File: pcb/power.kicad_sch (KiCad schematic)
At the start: 13 parts

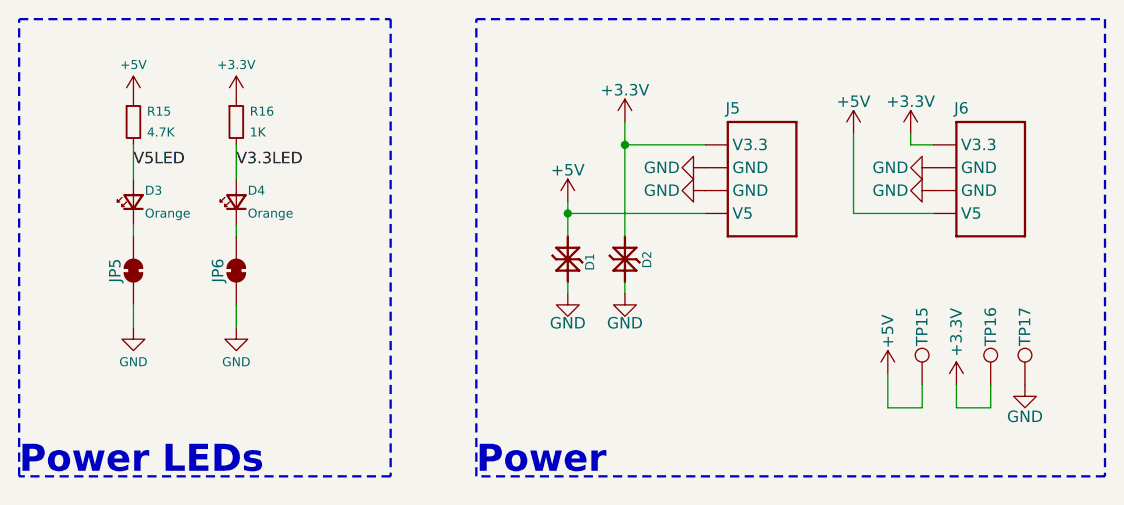
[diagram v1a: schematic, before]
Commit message: Redesign with cutouts for sensors
Removed power connectors since 5V is not needed
Added cutout for VOC sensor
Rerouted sensor section
Rescaled logos and fixed silkscreen
Changed to blue LED for power indicator
Updated requirements and renders
Changed all 0.1uF caps to small symbol
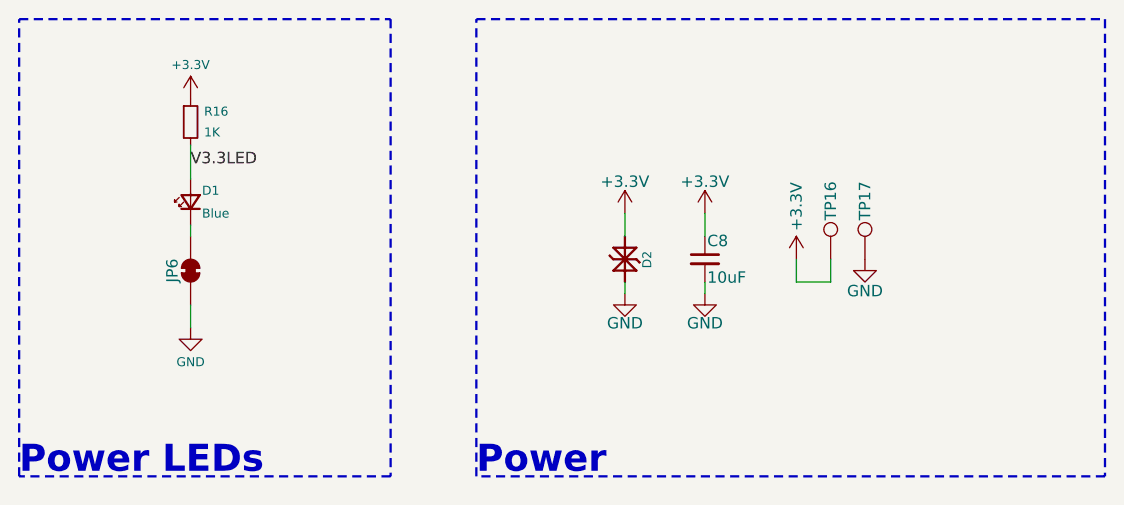
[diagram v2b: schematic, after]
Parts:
- removed D1: PESD5V5C1BL, CRGM Passive:DFN1006-2, symbol CRGM Passive:PESD5V5C1BLYL
- removed D3, D4: Orange, CRGM Passive:LED_0603_1608Metric, symbol Device:LED_Small
- removed J5, J6: ~, CRGM Connector:JST_SH_SM04B-SRSS-TB_1x04-1MP_P1.00mm_Horizontal, symbol CRGM Connector:AQ_POWER
- removed JP5: ~, CRGM Connector:SolderJumper-2_P1.3mm_Bridged_RoundedPad1.0x1.5mm, symbol Jumper:SolderJumper_2_Bridged
- removed R15: 4.7K, CRGM Passive:R_0603_1608Metric, symbol Device:R_Small
- removed TP15: ~, CRGM Mechanical:TestPoint_Pad_D1.0mm, symbol CRGM Connector:TestPoint
- added C8: 10uF, CRGM Passive:C_0603_1608Metric, symbol Device:C_Small
- added D1: Blue, CRGM Passive:LED_0603_1608Metric, symbol Device:LED_Small
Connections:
- net +3.3V: now also C8.1
- net GND: now also C8.2
- net V3.3LED: now also D1.2 (A)
- net at JP6.2 (B): now also D1.1 (K)
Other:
- moved on the sheet: JP6, R16, TP16, TP17

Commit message: Adjusted spacing and alignment of parts
Moved temp and voc to be on grid
Updated renders
Ran ERC -- fixed errors
Ran DRC -- fixed errors
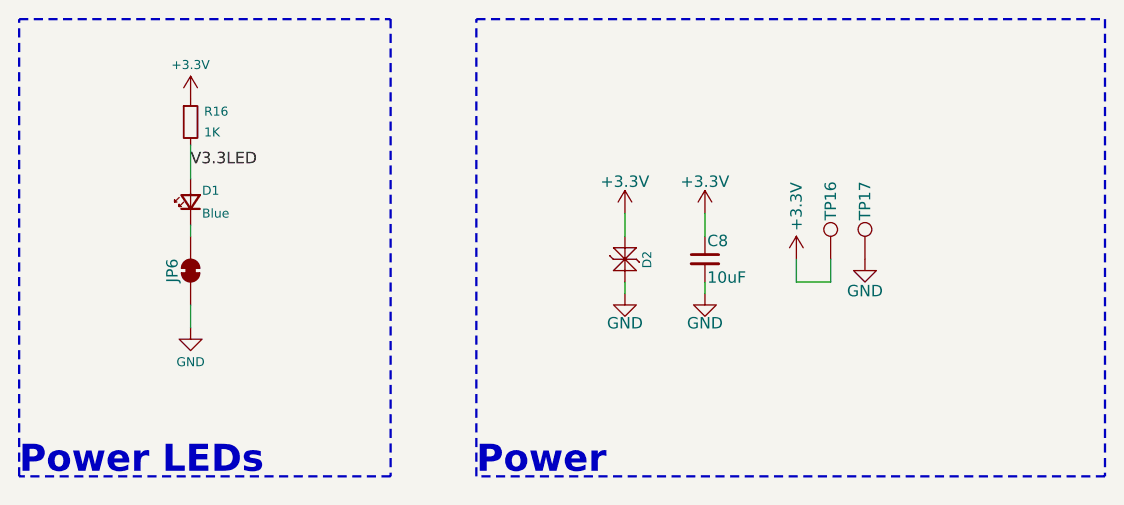
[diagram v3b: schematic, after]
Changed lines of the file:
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@@
+			)
+		)
+		(property "Sim.Pins" "1=K 2=A"
+			(at 44.45 45.72 0)
+			(effects
+				(font
+					(size 1.27 1.27)
+				)
+				(hide yes)
 			)
 		)
